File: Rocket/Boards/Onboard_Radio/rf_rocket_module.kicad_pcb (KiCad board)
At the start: 4 copper layers, 65 x 50 mm, 82 parts, among them J10 M80, J3 USB_B_Micro, J4 SWD JST PH, J5 Conn_01x08, J6 RFIO SMA, J7 CAN1_T, J8 CAN2_T, J9 M80, U1 TCAN1046, U2 SX1262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

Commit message: updates
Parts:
- moved R11 3.93 mm to (143.7, 125.2)
- moved R10 3.90 mm to (142.2, 125.2)
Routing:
- net Net-(U4-PA11): track 15.3 -> 0.00 mm
- net Net-(U4-PA12): track 13.5 -> 0.00 mm
- net /MCU/USB_D-: track 7.31 -> 3.36 mm
- net /MCU/USB_D+: track 7.19 -> 3.30 mm
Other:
- board text added: "Hybrid 26"
- board text added: "REV A"

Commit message: updates
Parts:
- removed R17, R18, R19: 0R, Resistor_SMD:R_0603_1608Metric
- added C35: 1uF, Capacitor_SMD:C_0603_1608Metric, F.Cu at (160.1, 144.7)
- added C36: 1uF, Capacitor_SMD:C_0603_1608Metric, F.Cu at (161.7, 147.0)
- added C37: 1uF, Capacitor_SMD:C_0603_1608Metric, F.Cu at (168.2, 147.0)
- added C38: 1uF, Capacitor_SMD:C_0603_1608Metric, F.Cu at (166.7, 144.7)
- added C39: 0.1uF, Capacitor_SMD:C_0603_1608Metric, F.Cu at (165.9, 161.1)
- added C40: 0.33uF, Capacitor_SMD:C_0603_1608Metric, F.Cu at (161.8, 157.6)
- added J11: MICROFIT, Connector_Molex:Molex_Micro-Fit_3.0_43045-0412_2x02_P3.00mm_Vertical, F.Cu at (152.3, 131.6)
- added JP3: SolderJumper, Jumper:SolderJumper-3_P1.3mm_Open_Pad1.0x1.5mm, F.Cu at (161.8, 126.8)
- added JP4: SolderJumper, Jumper:SolderJumper-3_P1.3mm_Open_Pad1.0x1.5mm, F.Cu at (166.6, 126.8)
- added JP6: SolderJumper, Jumper:SolderJumper-3_P1.3mm_Open_Pad1.0x1.5mm, F.Cu at (166.6, 129.4)
- added U5: MIC5365-3.3YC5, Package_TO_SOT_SMD:SOT-353_SC-70-5, F.Cu at (162.0, 144.7)
- added U6: MIC5365-3.3YC5, Package_TO_SOT_SMD:SOT-353_SC-70-5, F.Cu at (168.6, 144.7)
- added U7: AS78L05RTR-E1, Package_TO_SOT_SMD:SOT-89-3, F.Cu at (166.4, 156.2)
- J5: value Conn_01x08 -> MICROFIT; footprint Connector_PinSocket_2.54mm:PinSocket_1x08_P2.54mm_Vertical -> Connector_Molex:Molex_Micro-Fit_3.0_43045-0412_2x02_P3.00mm_Vertical
- moved R20 44.8 mm to (196.9, 149.4)
- moved H3 42.5 mm to (220.0, 112.5)
- moved J4 25.0 mm to (187.6, 107.4), turned to 0 degrees
- moved J5 8.05 mm to (176.0, 131.7), turned to 0 degrees
- moved J3 6.59 mm to (137.9, 135.6)
- moved R10 6.39 mm to (136.9, 128.8)
- moved R11 6.39 mm to (138.4, 128.8)
- moved H4 3.75 mm to (187.0, 134.0)
- moved H1 3.75 mm to (128.0, 90.0)
- moved H2 3.70 mm to (128.0, 134.0)
- moved C23 2.21 mm to (164.6, 103.1)
- moved C24 2.08 mm to (163.0, 101.8)
- moved F2 1.34 mm to (133.3, 125.6), turned to 90 degrees
- moved C28 1.04 mm to (154.2, 117.8), turned to 90 degrees
- moved C27 0.98 mm to (152.7, 116.1), turned to 90 degrees
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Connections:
- net Net-(U4-PA11) renamed /MCU/MCU_D-
- net Net-(U4-PA12) renamed /MCU/MCU_D+
- J5 pad 1: GND -> /Power Input/+V_In
- J5 pad 2: unconnected-(J5-Pin_2-Pad2) -> GND
- J5 pad 3: unconnected-(J5-Pin_3-Pad3) -> GND
- R20 pad 1: /Power Input/+7V4 -> /Power Input/+7V4_In
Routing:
- net /MCU/SWCLK: track 34.9 -> 0.00 mm, vias 2 -> 0
- net /MCU/SWDIO: track 31.2 -> 0.00 mm, vias 2 -> 0
- net /MCU/MCU_D-: track 0.00 -> 25.2 mm
- net /MCU/MCU_D+: track 0.00 -> 24.5 mm
- net /MCU/NRST: track 22.1 -> 0.00 mm, vias 2 -> 0
- net VDD_RADIO: track 48.3 -> 41.5 mm
- net /Power Input/+5V: track 2.56 -> 0.00 mm
- net /Power Input/+3V3A: track 2.53 -> 0.00 mm
- net /Power Input/+3V3: track 2.53 -> 0.00 mm
- net GND: track 47.0 -> 44.6 mm, vias 48 -> 44
- net +5V: track 31.0 -> 28.7 mm, vias 3 -> 2
- net +7V4: track 49.1 -> 51.3 mm, vias 3 -> 2
- net +3V3: track 17.8 -> 16.7 mm, vias 12 -> 13
- net /CAN_Termination/CANH1: track 34.3 -> 35.0 mm
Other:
- outline, holes or cut-outs redrawn

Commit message: everything minus trace impedance and via stictching
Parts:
- removed J7: CAN1_T, Connector_PinHeader_2.54mm:PinHeader_1x02_P2.54mm_Vertical
- removed J8: CAN2_T, Connector_PinHeader_2.54mm:PinHeader_1x02_P2.54mm_Vertical
- removed JP1, JP2: CH SEL, Jumper:SolderJumper-3_P1.3mm_Bridged12_RoundedPad1.0x1.5mm
- removed R2: 100K, Resistor_SMD:R_0603_1608Metric
- added JP5: SolderJumper_2_Open, Jumper:SolderJumper-2_P1.3mm_Open_RoundedPad1.0x1.5mm, F.Cu at (134.0, 104.7)
- added JP7: SolderJumper_2_Open, Jumper:SolderJumper-2_P1.3mm_Open_RoundedPad1.0x1.5mm, F.Cu at (134.0, 117.6)
- added JP8: CH SEL, Jumper:SolderJumper-3_P1.3mm_Open_RoundedPad1.0x1.5mm, F.Cu at (134.0, 113.5)
- added JP9: CH SEL, Jumper:SolderJumper-3_P1.3mm_Open_RoundedPad1.0x1.5mm, F.Cu at (134.0, 108.8)
- D2: value LED_G -> LED_R
- D3: value LED_R -> LED_G
- H1, H2, H3, H4: footprint MountingHole:MountingHole_3.2mm_M3 -> MountingHole:MountingHole_3.2mm_M3_DIN965_Pad
- J10, J9: footprint Connector_Harwin:Harwin_LTek-Male_2x05_P2.00mm_Vertical -> Library:HARWIN_M80-5011005
- JP3, JP4, JP6: footprint Jumper:SolderJumper-3_P1.3mm_Open_Pad1.0x1.5mm -> Jumper:SolderJumper-3_P1.3mm_Open_RoundedPad1.0x1.5mm
- U3: footprint Package_TO_SOT_SMD:Vishay_PowerPAK_SC70-6L_Dual -> Package_TO_SOT_SMD:SOT-363_SC-70-6
- moved D1 51.1 mm to (134.1, 134.9), turned to 90 degrees
- moved D2 49.7 mm to (137.3, 134.9), turned to 90 degrees
- moved D3 48.8 mm to (140.3, 134.9), turned to 90 degrees
- moved R16 47.0 mm to (137.3, 131.9), turned to -90 degrees
- moved R14 47.0 mm to (134.1, 131.8), turned to -90 degrees
- moved R15 42.9 mm to (140.3, 131.9), turned to -90 degrees
- moved C40 38.6 mm to (182.4, 124.9)
- moved R20 38.6 mm to (167.2, 124.9)
- moved C39 37.1 mm to (174.2, 124.9)
- moved U7 35.0 mm to (179.1, 123.5)
- moved H3 34.7 mm to (186.4, 103.8)
- moved U5 29.6 mm to (177.7, 119.7)
- moved C35 27.7 mm to (175.7, 121.8)
- moved C36 26.2 mm to (175.7, 124.9), turned to 90 degrees
- moved C38 25.0 mm to (169.8, 119.9), turned to 180 degrees
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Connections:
- C16 pad 1: VDD_RADIO -> /+3V3A
- C18 pad 1: VDD_RADIO -> /+3V3A
- C38 pad 1: Net-(U6-VOUT) -> /+3V3A
- R15 pad 2: Net-(D2-A) -> Net-(D3-A)
- R16 pad 2: Net-(D3-A) -> Net-(D2-A)
- U2 pad 1: VDD_RADIO -> /+3V3A
- U2 pad 10: VDD_RADIO -> /+3V3A
- U2 pad 11: VDD_RADIO -> /+3V3A
- U4 pad 14: /MCU/LED1 -> unconnected-(U4-PA0-Pad14)
- U4 pad 15: /MCU/LED2 -> unconnected-(U4-PA1-Pad15)
- U4 pad 2: unconnected-(U4-PC13-Pad2) -> /MCU/3V3A_LDO_EN
- U4 pad 3: unconnected-(U4-PC14-Pad3) -> /MCU/3V3_LDO_EN
- U4 pad 51: unconnected-(U4-PC10-Pad51) -> /MCU/LED2
- U4 pad 52: unconnected-(U4-PC11-Pad52) -> /MCU/LED1
- U5 pad 3: /Power Input/3V3_LDO_EN -> /MCU/3V3_LDO_EN
- U6 pad 3: /Power Input/3V3A_LDO_EN -> /MCU/3V3A_LDO_EN
- U6 pad 5: Net-(U6-VOUT) -> /+3V3A
- U7 pad 1: /Power Input/+V_In -> /Power Input/+5V_LDO
- U7 pad 3: /Power Input/5V_LDO_EN -> /Power Input/+V_In
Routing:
- net /+3V3A: track 0.00 -> 48.1 mm, vias 0 -> 3
- net VDD_RADIO: track 41.5 -> 0.00 mm, vias 3 -> 0
- net /MCU/SWCLK: track 0.00 -> 35.0 mm, vias 0 -> 2
- net /MCU/SWDIO: track 0.00 -> 33.6 mm, vias 0 -> 2
- net +5V: track 28.7 -> 52.3 mm, vias 2 -> 3
- net /MCU/NRST: track 0.00 -> 23.5 mm, vias 0 -> 2
- net /Power Input/+3V3_In: track 0.00 -> 21.4 mm, vias 0 -> 1
- net /Power Input/+5V_In: track 0.00 -> 19.1 mm, vias 0 -> 2
- net /MCU/3V3_LDO_EN: track 0.00 -> 16.3 mm, vias 0 -> 2
- net /MCU/LED2: track 11.1 -> 27.2 mm, vias 0 -> 2
- net /MCU/LED1: track 10.2 -> 24.8 mm, vias 0 -> 2
- net /Power Input/+5V_LDO: track 0.00 -> 14.0 mm
- net GND: track 44.6 -> 58.5 mm, vias 44 -> 52
- net /MCU/3V3A_LDO_EN: track 0.00 -> 13.1 mm, vias 0 -> 2
- net +7V4: track 51.3 -> 38.4 mm
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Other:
- outline, holes or cut-outs redrawn
- board text added: "+7V4"
- board text added: "2S BAT IN"
- board text added: "CAN1"
- board text added: "CAN2"
- board text added: "LED1"
- board text added: "LED2"
- board text added: "POWER IN"
- board text added: "SMA"
- board text added: "SWD"
- board text added: "USB IN"

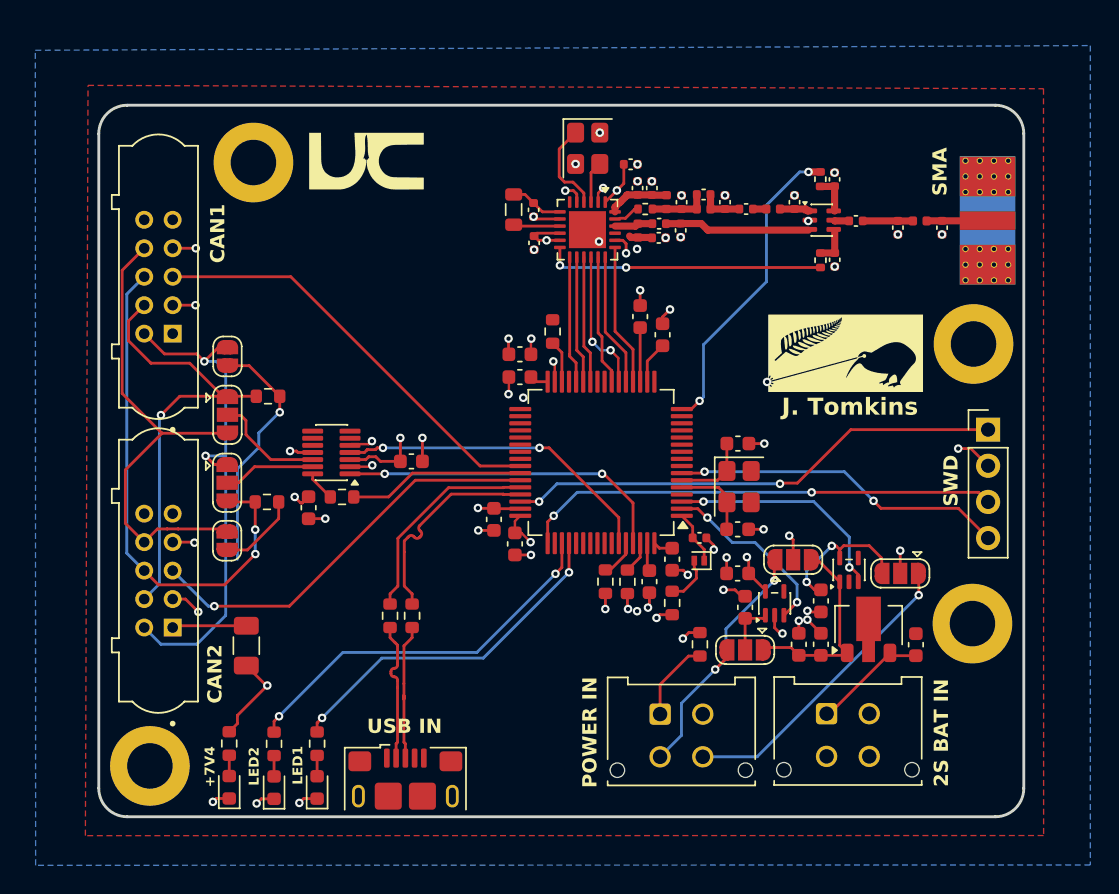
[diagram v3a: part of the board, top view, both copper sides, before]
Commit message: rf traces updated, need to workout board net class
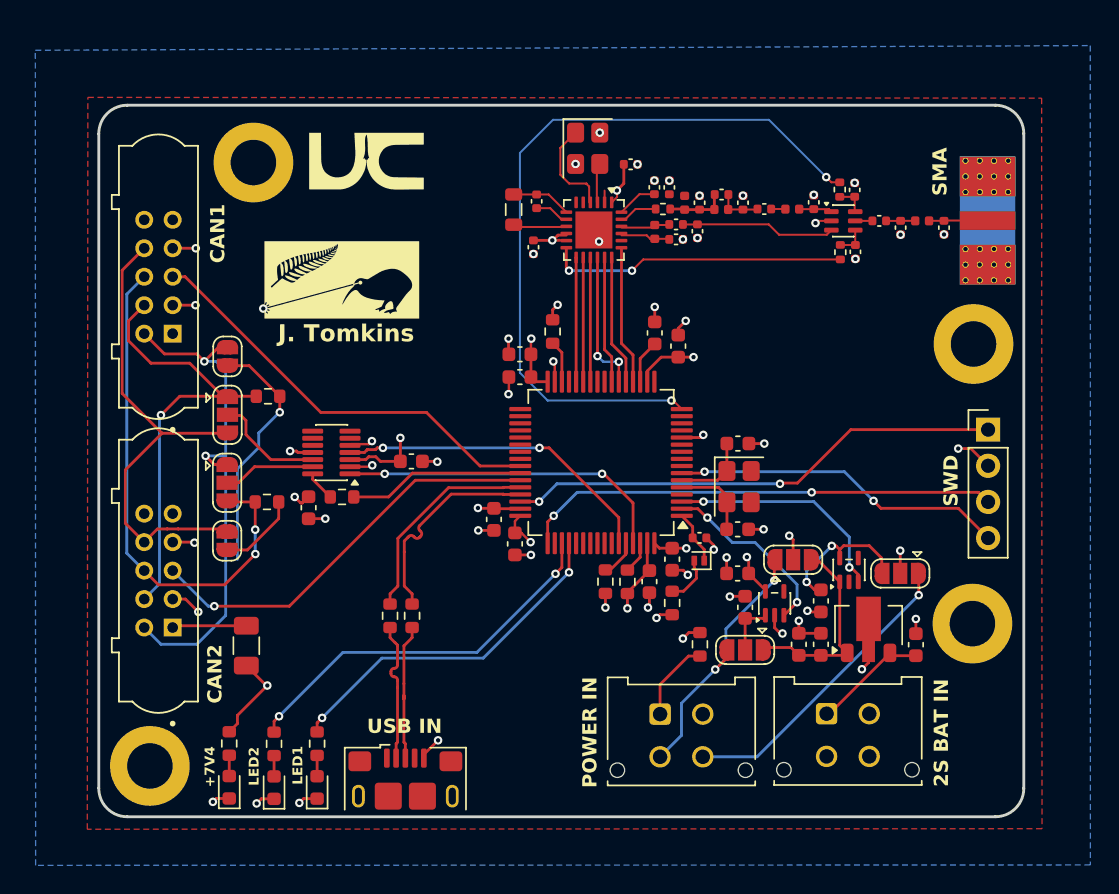
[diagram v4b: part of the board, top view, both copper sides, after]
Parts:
- moved C8 1.64 mm to (179.8, 95.1)
- moved C14 1.59 mm to (178.1, 93.0)
- moved C15 1.56 mm to (178.1, 97.3)
- moved R4 1.55 mm to (177.0, 92.9)
- moved C24 1.54 mm to (164.0, 103.0)
- moved U3 1.51 mm to (177.3, 95.1)
- moved R3 1.51 mm to (177.1, 97.3)
- moved C23 1.36 mm to (165.7, 103.9)
- moved C7 1.35 mm to (175.2, 93.8)
- moved L4 1.34 mm to (173.7, 94.3)
- moved L1 1.28 mm to (166.1, 93.8)
- moved C6 1.28 mm to (171.7, 94.3)
- moved C3 1.27 mm to (167.2, 93.8)
- moved C5 1.26 mm to (170.2, 93.8)
- moved C4 1.26 mm to (168.7, 93.3)
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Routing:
- net /LoRav2/ANT_SW: track 21.9 -> 53.1 mm
- net GND: track 58.5 -> 68.1 mm, vias 52 -> 51
- net Net-(U2-RFI_P): track 1.63 -> 3.48 mm
- net Net-(U2-VR_PA): track 4.33 -> 2.84 mm
- net Net-(C8-Pad2): track 3.54 -> 2.05 mm
- net /LoRav2/DIO2: track 19.6 -> 21.1 mm
- net Net-(U2-RFO): track 1.55 -> 2.49 mm
- net Net-(U2-RFI_N): track 2.69 -> 3.45 mm
- net Net-(U3-RF_2): track 10.2 -> 10.9 mm
- net Net-(U3-VDD): track 2.74 -> 2.11 mm

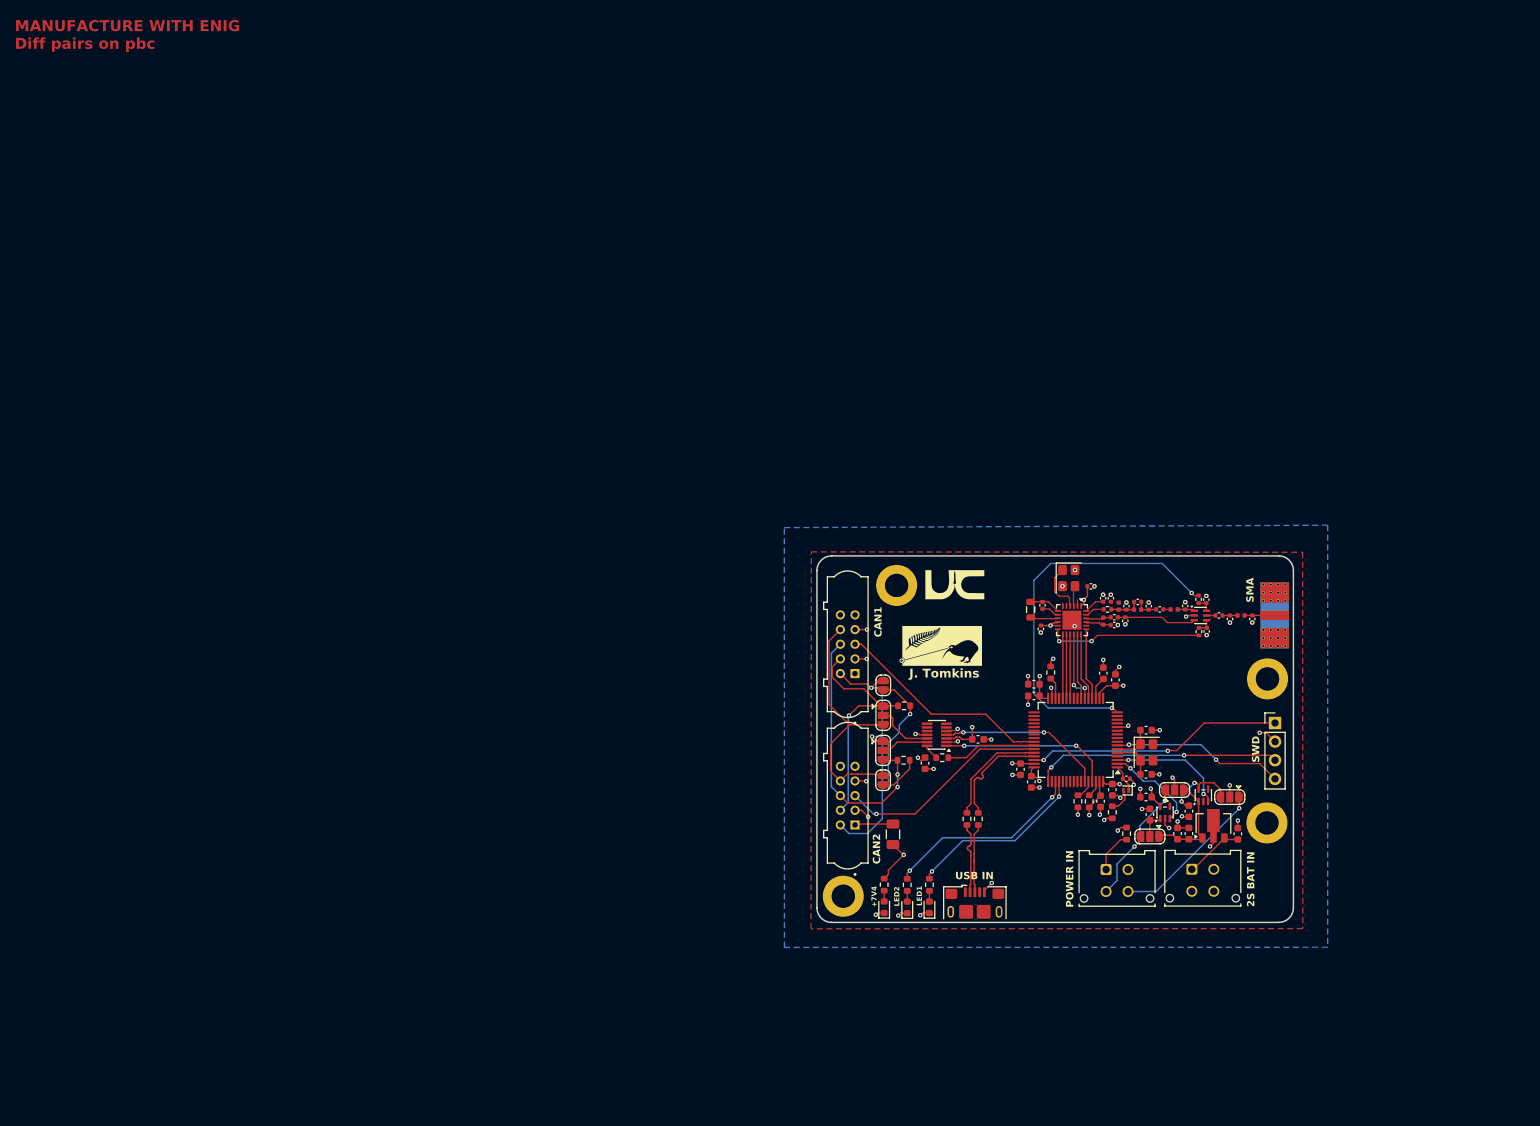
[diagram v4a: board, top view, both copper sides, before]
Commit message: via fencing done, need via stiching
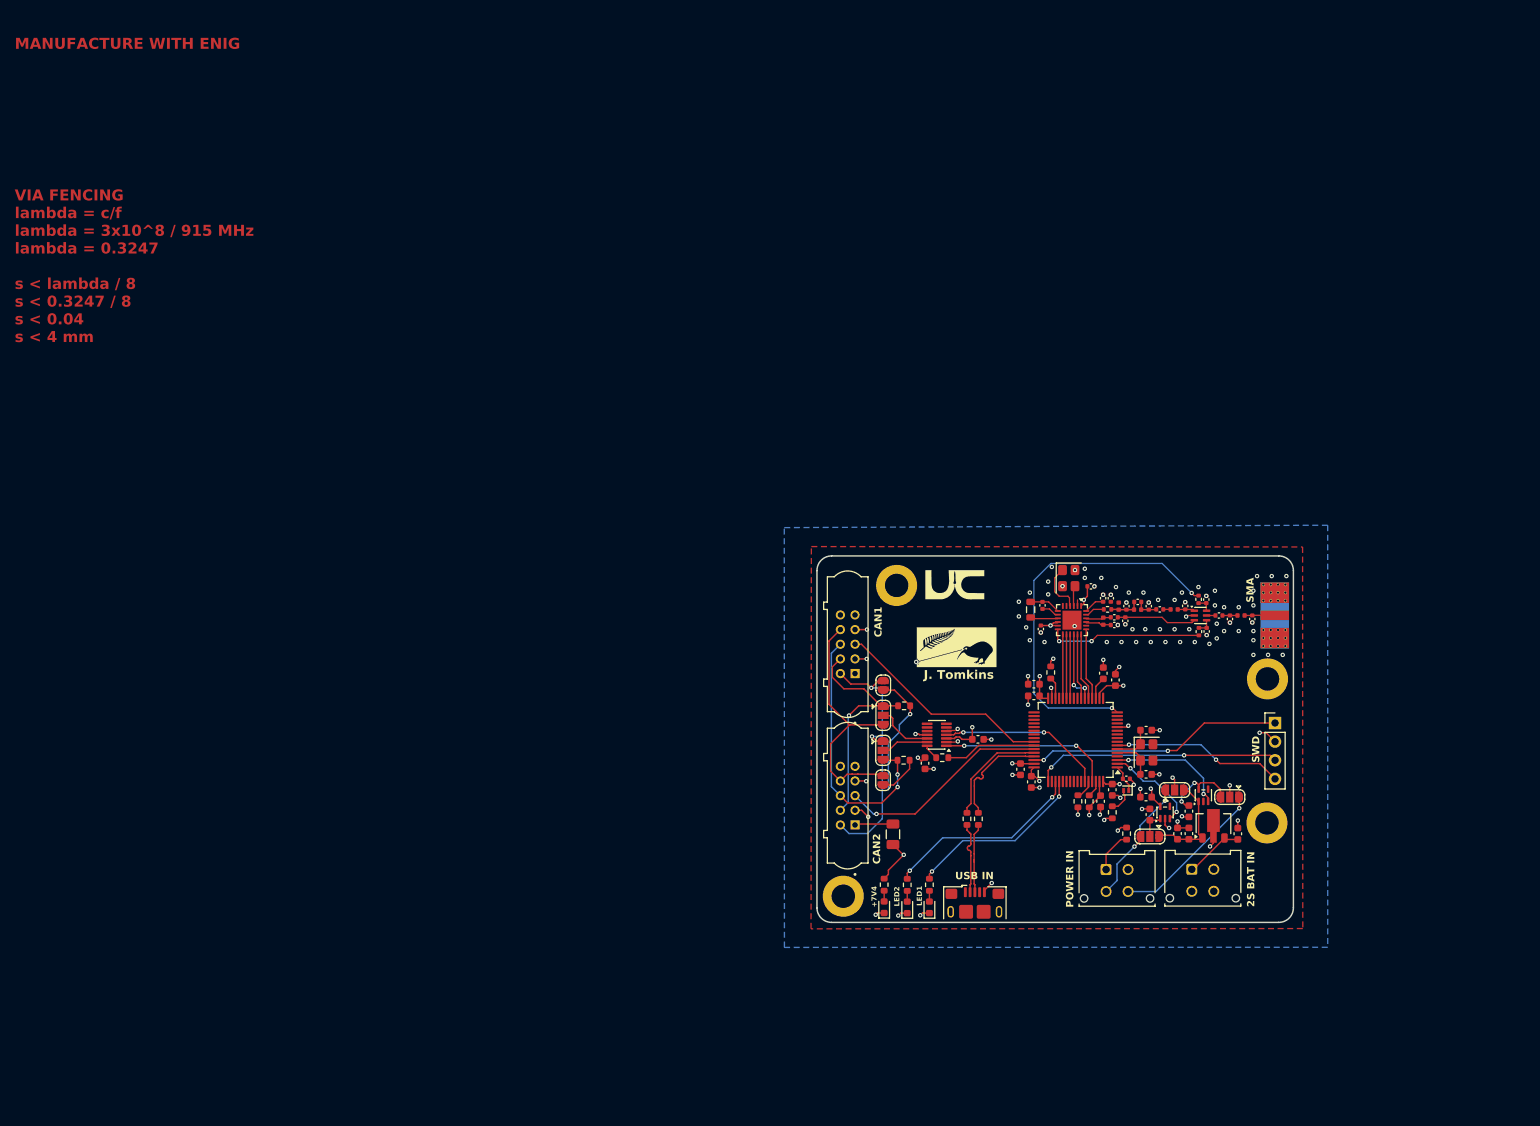
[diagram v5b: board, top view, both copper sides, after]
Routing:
- net GND: vias 51 -> 101
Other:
- board text added: "MANUFACTURE WITH ENIG"
- board text added: "VIA FENCING lambda = c/f lambda = 3x10^8 / 915 MHz lambda = 0.3247 s < lambda / 8 s < 0.3247 / 8 s < 0.04 s < 4 mm"
- board text removed: "MANUFACTURE WITH ENIG Diff pairs on pbc"

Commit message: needs pcb and schematic review
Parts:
- C39: value 0.1uF -> 100nF
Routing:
- net Net-(JP5-A): track 17.3 -> 4.57 mm, vias 1 -> 0
- net GND: track 68.1 -> 71.5 mm, vias 101 -> 122
- net Net-(U2-VR_PA): track 2.84 -> 5.01 mm
